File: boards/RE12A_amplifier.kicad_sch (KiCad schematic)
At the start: 14 parts, among them J14 RE12A, J15 Conn_01x03 encoder_direct, Q1 NPN, U3 MOUDLE-SEEEDUINO-XIAO-ESP32C3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, U7 LM397

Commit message: DRCエラー解消
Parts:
- added Batt5: Conn_01x02, Connector_JST:JST_PH_S2B-PH-SM4-TB_1x02-1MP_P2.00mm_Horizontal, symbol Connector_Generic:Conn_01x02
- J15: value Conn_01x03 encoder_direct -> encoder_direct
- U7: value LM397 -> TJ393
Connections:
- net +3.3V-3 is gone; now on net +3.3V-4: J15.1 (Pin_1), U7.8 (V+)
- net GND-3 is gone; now on net GND-4: J15.2 (Pin_2), U7.4 (V-)
- net +BATT-4: now also Batt5.1 (Pin_1)
- net GND-4: now also Batt5.2 (Pin_2)
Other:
- moved on the sheet: Q1, R16, R19, R21

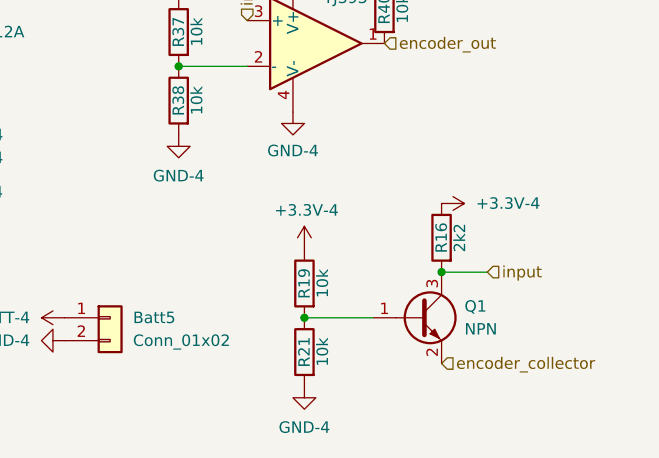
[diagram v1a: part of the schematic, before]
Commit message: 動作確認をもとに統合版コード修正
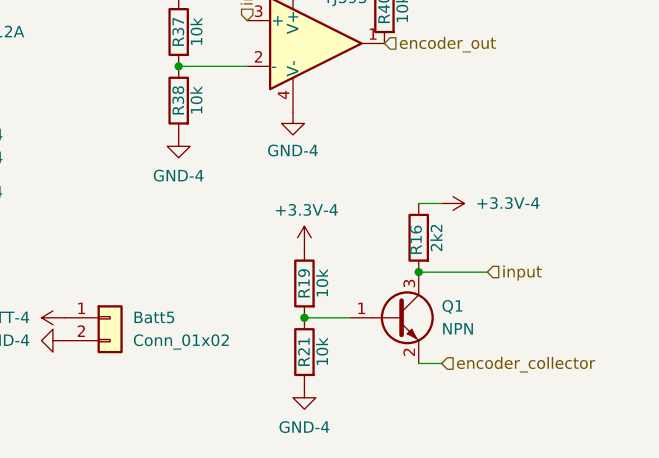
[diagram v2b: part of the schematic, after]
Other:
- moved on the sheet: Q1, R16
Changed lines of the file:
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@@
 	(paper "A4")
+	(junction
+		(at 217.17 132.08)
+		(diameter 0)
+		(color 0 0 0 0)
+	)
 	(junction
 		(at 204.47 137.16)
@@
 		(color 0 0 0 0)
 	)
-	(junction
-		(at 219.71 132.08)
-		(diameter 0)
-		(color 0 0 0 0)
-	)
 	(no_connect
 		(at 138.43 39.37)
@@
 	(wire
 		(pts
-			(xy 224.79 132.08) (xy 219.71 132.08)
+			(xy 190.5 109.22) (xy 198.12 109.22)
 		)
 		(stroke
@@
 	(wire
 		(pts
-			(xy 190.5 109.22) (xy 198.12 109.22)
+			(xy 217.17 142.24) (xy 219.71 142.24)
 		)
 		(stroke
@@
 	(wire
 		(pts
-			(xy 200.66 82.55) (xy 201.93 82.55)
+			(xy 217.17 132.08) (xy 224.79 132.08)
 		)
 		(stroke
@@
 	(wire
 		(pts
-			(xy 204.47 137.16) (xy 212.09 137.16)
+			(xy 204.47 137.16) (xy 209.55 137.16)
+		)
+		(stroke
+			(width 0)
+			(type default)
+		)
+	)
+	(wire
+		(pts
+			(xy 200.66 82.55) (xy 201.93 82.55)
+		)
+		(stroke
+			(width 0)
+			(type default)
+		)
+	)
+	(wire
+		(pts
+			(xy 217.17 124.46) (xy 219.71 124.46)
 		)
 		(stroke
@@
 	(symbol
 		(lib_id "Transistor_BJT:MMBT2222A")
-		(at 217.17 137.16 0)
+		(at 214.63 137.16 0)
 		(unit 1)
 		(exclude_from_sim no)
@@
 		(fields_autoplaced yes)
 		(property "Reference" "Q1"
-			(at 222.25 135.8899 0)
+			(at 219.71 135.8899 0)
 			(effects
 				(font
@@
 		)
 		(property "Value" "NPN"
-			(at 222.25 138.4299 0)
+			(at 219.71 138.4299 0)
 			(effects
 				(font
@@
 		)
 		(property "Footprint" "Package_TO_SOT_SMD:SOT-23"
-			(at 222.25 139.065 0)
+			(at 219.71 139.065 0)
 			(effects
 				(font
@@
 		)
 		(property "Datasheet" "https://assets.nexperia.com/documents/data-sheet/MMBT2222A.pdf"
-			(at 217.17 137.16 0)
+			(at 214.63 137.16 0)
 			(effects
 				(font
@@
 		)
 		(property "Description" "600mA Ic, 40V Vce, NPN Transistor, SOT-23"
-			(at 217.17 137.16 0)
+			(at 214.63 137.16 0)
 			(effects
 				(font
@@
 		)
 		(property "Sim.Device" "NPN"
-			(at 217.17 137.16 0)
+			(at 214.63 137.16 0)
 			(effects
 				(font
@@
 		)
 		(property "Sim.Type" "GUMMELPOON"
-			(at 217.17 137.16 0)
+			(at 214.63 137.16 0)
 			(effects
 				(font
@@
 		)
 		(property "Sim.Pins" "1=C 2=B 3=E"
-			(at 217.17 137.16 0)
+			(at 214.63 137.16 0)
 			(effects
 				(font
@@
 	(symbol
 		(lib_id "Device:R")
-		(at 219.71 128.27 0)
+		(at 217.17 128.27 0)
 		(mirror y)
 		(unit 1)
@@
 		(dnp no)
 		(property "Reference" "R16"
-			(at 219.71 128.27 90)
+			(at 216.916 128.524 90)
 			(effects
 				(font
@@
 		)
 		(property "Value" "2k2"
-			(at 221.742 128.27 90)
+			(at 219.202 128.27 90)
 			(effects
 				(font
@@
 		)
 		(property "Footprint" "Resistor_SMD:R_0603_1608Metric_Pad0.98x0.95mm_HandSolder"
-			(at 221.488 128.27 90)
+			(at 218.948 128.27 90)
 			(effects
 				(font
@@
 		)
 		(property "Datasheet" "~"
-			(at 219.71 128.27 0)
+			(at 217.17 128.27 0)
 			(effects
 				(font
@@
 		)
 		(property "Description" "Resistor"
-			(at 219.71 128.27 0)
-			(effects
-				(font
+			(at 217.17 128.27 0)
+			(effects
+				(font
